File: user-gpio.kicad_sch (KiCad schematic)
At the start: 96 parts, among them J10 62732020621, J11 62703420621, J4 BM04B-SRSS-TB-LF-SN, J5 SSW-106-02-G-D-RA, J6 SSW-106-02-G-D-RA, J7 BM04B-SRSS-TB-LF-SN, J8 BM04B-SRSS-TB-LF-SN, J9 62704020621, Q10 BSS138PW, Q11 BSS138PW, Q12 IRLML6344TRPBF, Q13 BSS138PW, Q14 BSS138PW, Q15 BSS138PW, Q16 BSS138PW, Q8 BSS138PW, Q9 BSS138PW, SW2 CVS-08TB, U45 TPD4E05U06QDQARQ1, U46 TPD4E05U06QDQARQ1

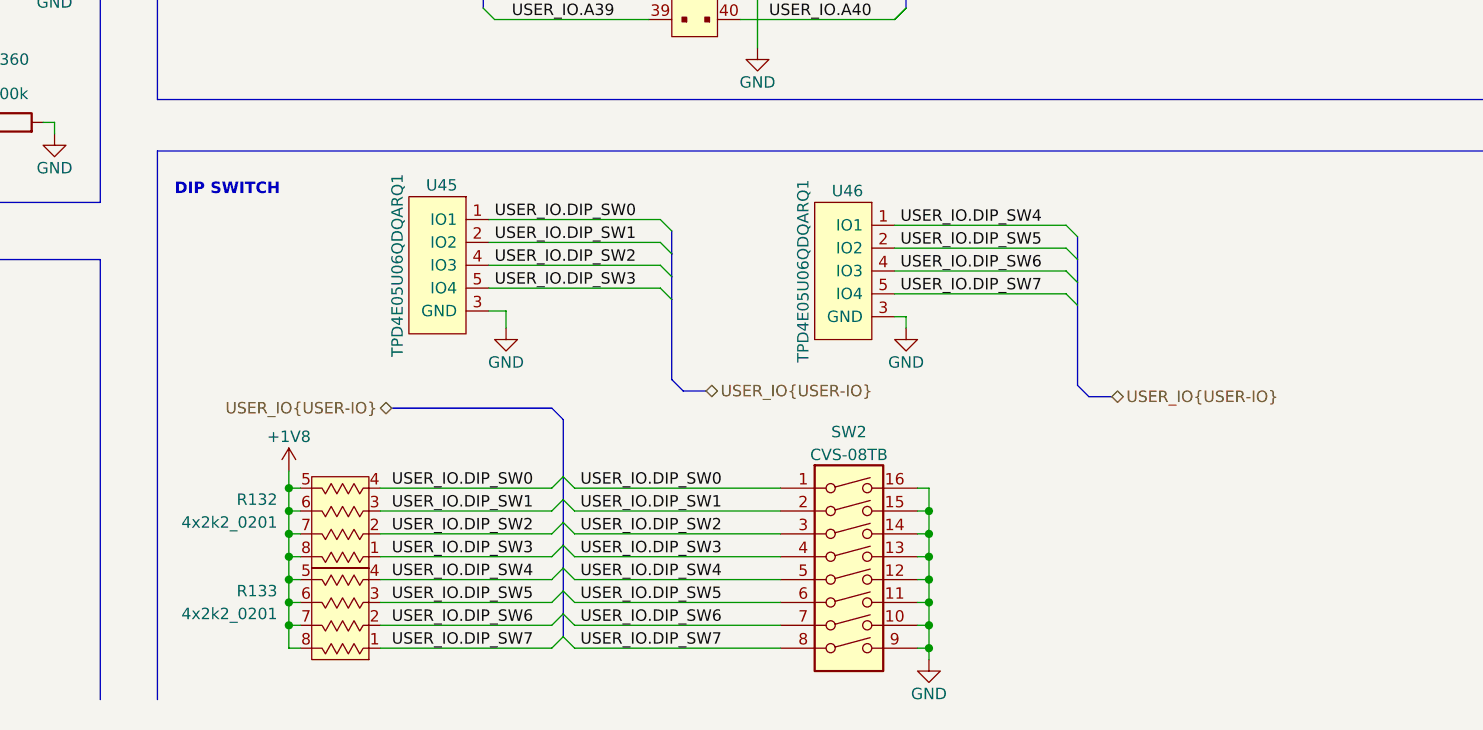
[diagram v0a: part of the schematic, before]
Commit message: Updated all symbols causing warnings with no signal connected to pad, added thermal vias on level shifters' thermal pad with small tweaks on signal routing near this area
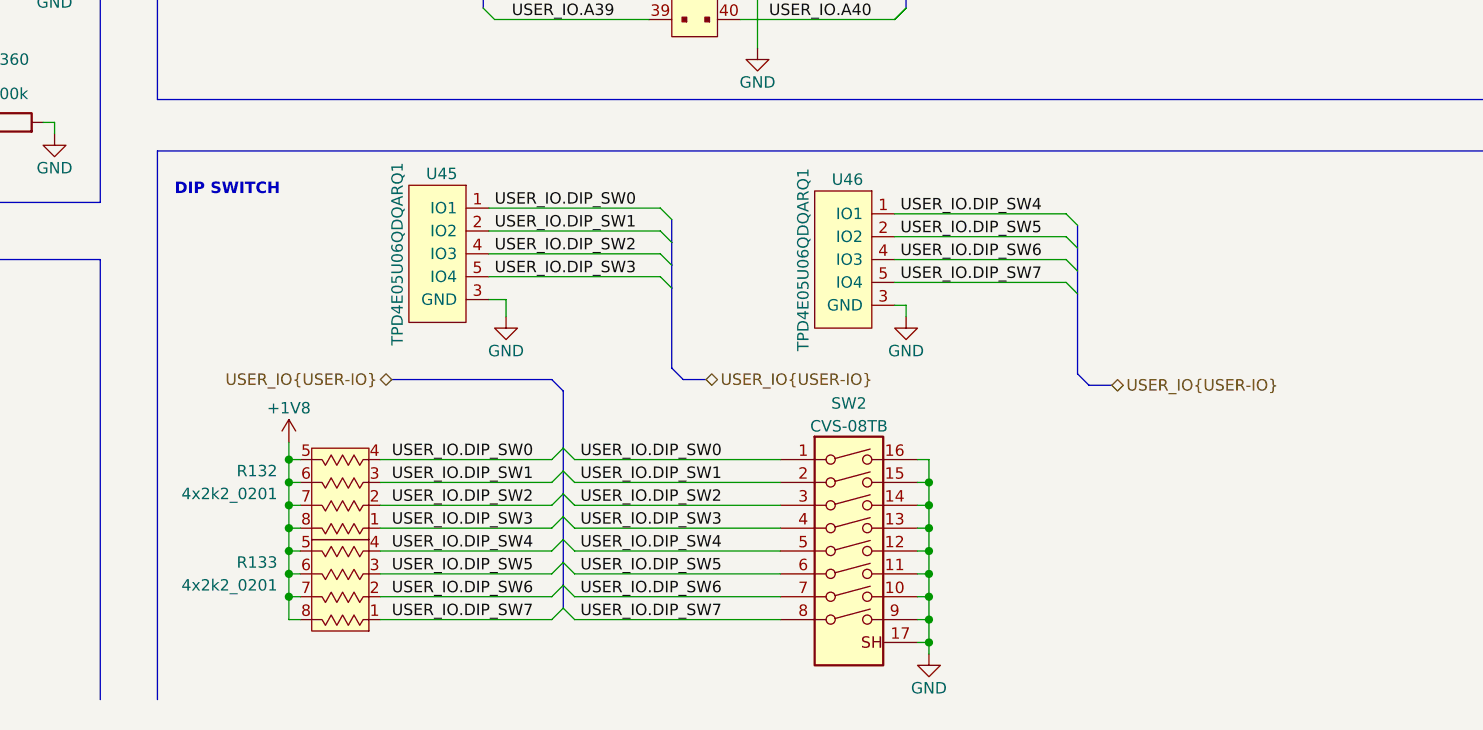
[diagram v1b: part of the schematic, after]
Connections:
- net GND: now also SW2.17 (SH)
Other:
- moved on the sheet: R132, R133, U45, U46
